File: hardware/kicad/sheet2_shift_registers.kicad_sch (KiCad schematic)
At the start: 0 parts

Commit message: feat: populate all 4 KiCad schematic sheets with embedded symbols and wiring
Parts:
- added U1, U2, U3, U4, U5, U6, U7, U8: 74HC595, symbol HPVE:74HC595
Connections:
- new net +3V3: U1.14 (SER), U2.14 (SER), U3.14 (SER), U4.14 (SER), U5.14 (SER), U6.14 (SER), U7.14 (SER), U8.14 (SER)
- new net CASCADE_1: U2.10 (~{SRCLR})
- new net CASCADE_2: U3.10 (~{SRCLR})
- new net CASCADE_3: U4.10 (~{SRCLR})
- new net CASCADE_4: U5.10 (~{SRCLR})
- new net CASCADE_5: U6.10 (~{SRCLR})
- new net CASCADE_6: U7.10 (~{SRCLR})
- new net CASCADE_7: U8.10 (~{SRCLR})
- new net GND: U1.11 (SRCLK), U2.11 (SRCLK), U3.11 (SRCLK), U4.11 (SRCLK), U5.11 (SRCLK), U6.11 (SRCLK), U7.11 (SRCLK), U8.11 (SRCLK)
- new net SPI_LATCH: U1.12 (RCLK), U2.12 (RCLK), U3.12 (RCLK), U4.12 (RCLK), U5.12 (RCLK), U6.12 (RCLK), U7.12 (RCLK), U8.12 (RCLK)
- new net SPI_MOSI: U1.10 (~{SRCLR})
- new net SPI_SCK: U1.13 (~{OE}), U2.13 (~{OE}), U3.13 (~{OE}), U4.13 (~{OE}), U5.13 (~{OE}), U6.13 (~{OE}), U7.13 (~{OE}), U8.13 (~{OE})
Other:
- title: Sheet 2: 74HC595 Shift Register Cascade -> Sheet 2: 74HC595 High-Speed Shift Register Cascade (8 Stages)

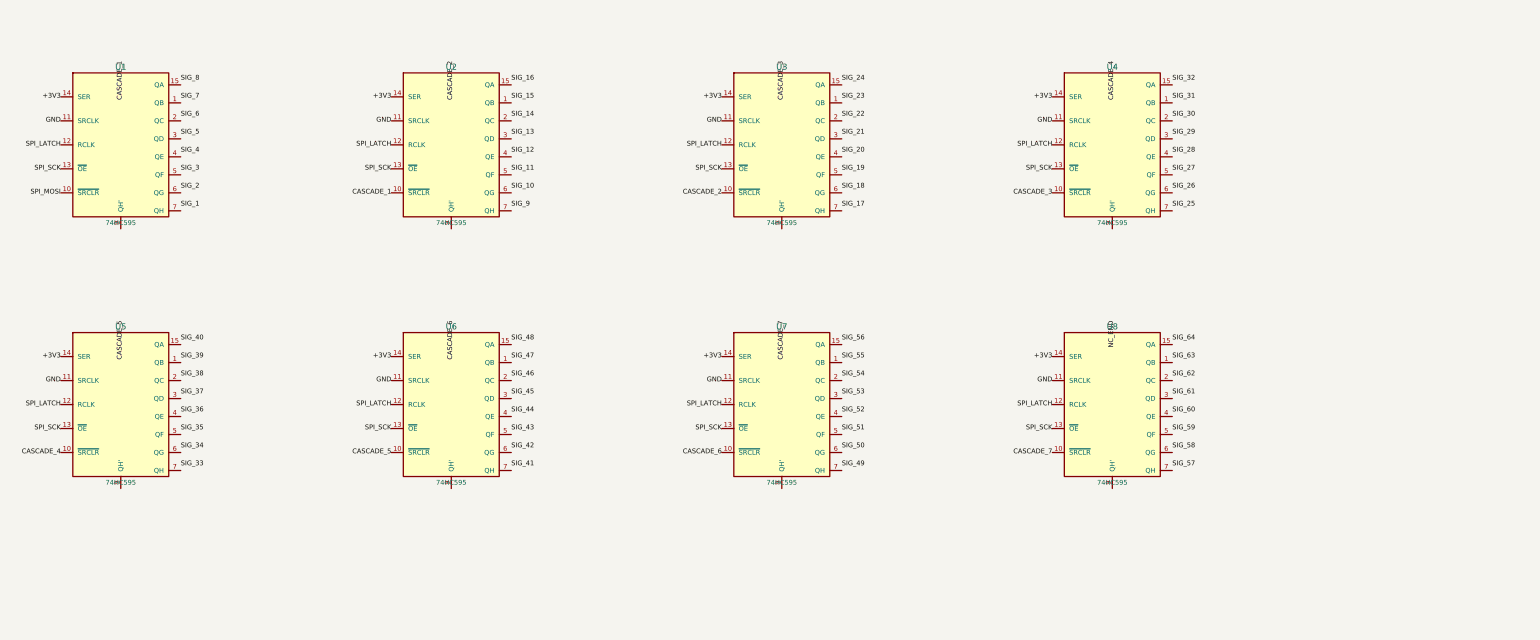
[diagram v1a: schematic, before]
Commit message: fix(kicad): assign valid footprints to all 105 symbols and add visible wiring
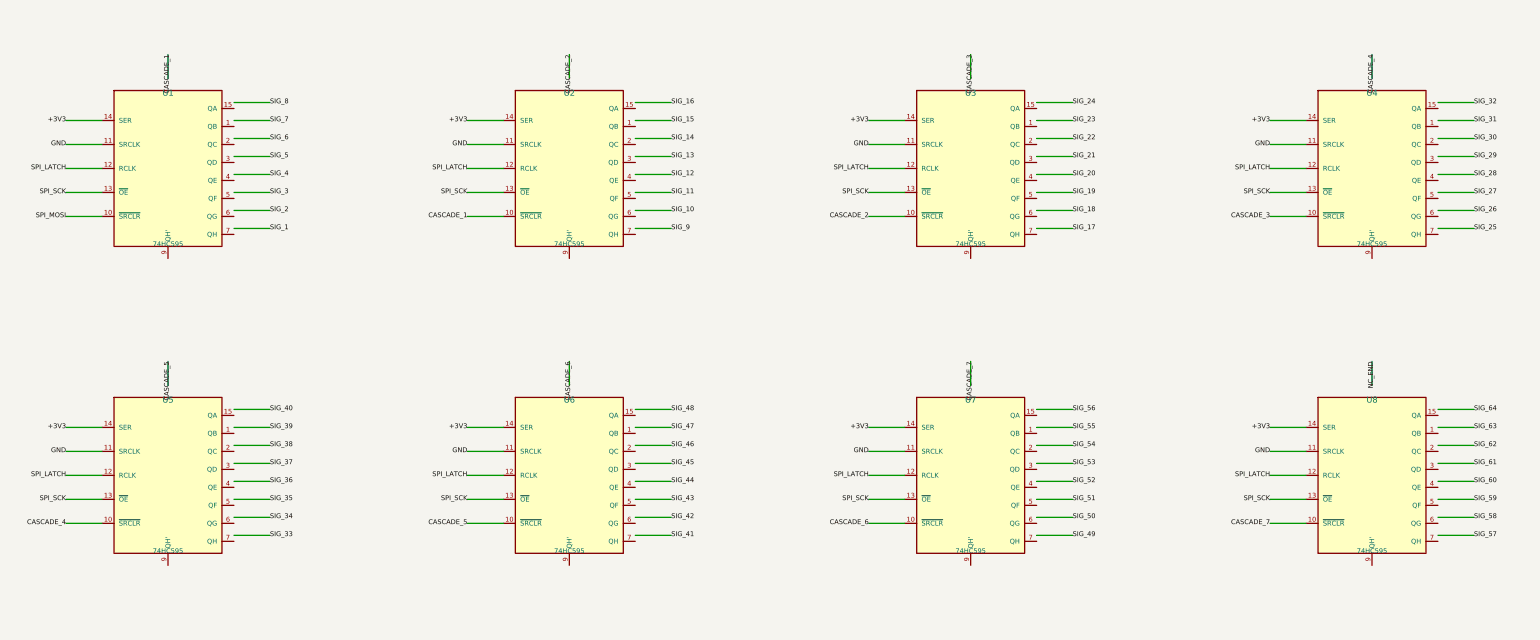
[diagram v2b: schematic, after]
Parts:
- U1, U2, U3, U4, U5, U6, U7, U8: footprint (none) -> Package_DIP:DIP-16_W7.62mm

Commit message: Update KiCad symbols and netlist for spotless F8 PCB sync
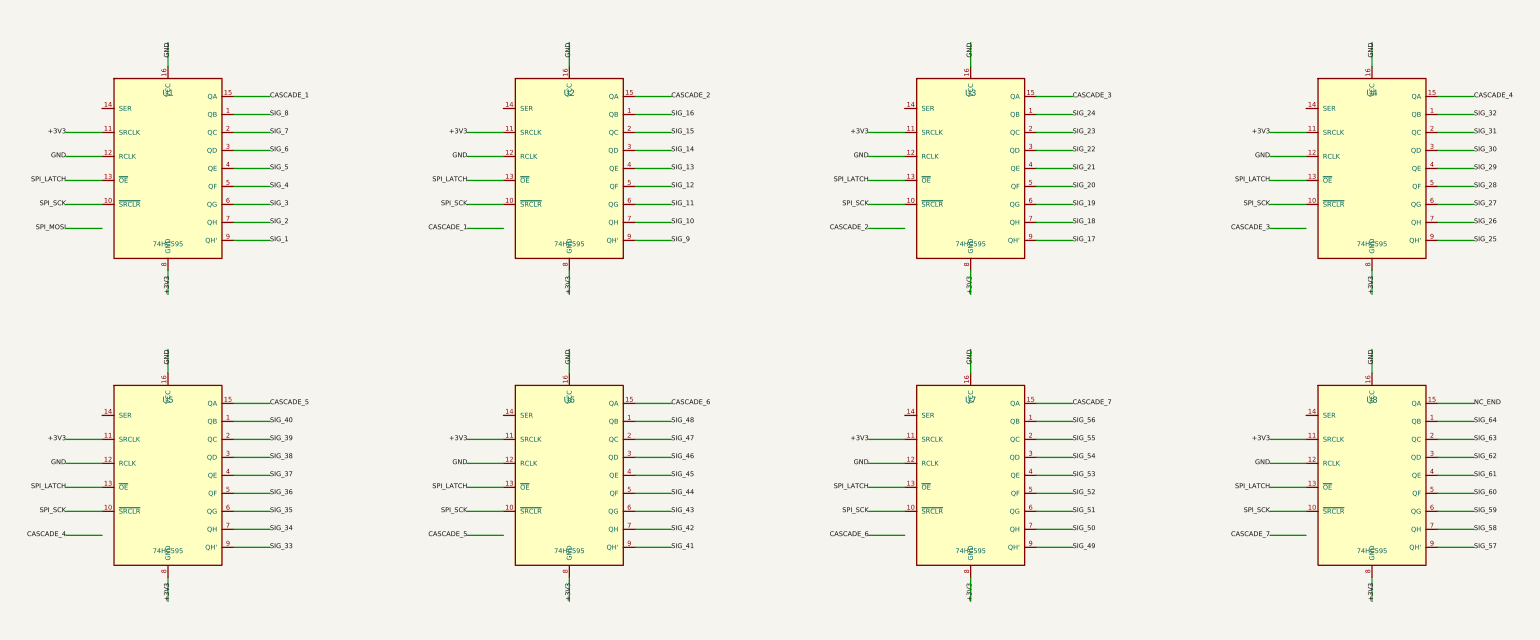
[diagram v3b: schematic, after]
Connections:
- net +3V3: now also U1.11 (SRCLK), U1.8 (GND), U2.11 (SRCLK), U2.8 (GND), U3.11 (SRCLK), U3.8 (GND), U4.11 (SRCLK), U4.8 (GND), U5.11 (SRCLK), U5.8 (GND), U6.11 (SRCLK), U6.8 (GND), U7.11 (SRCLK), U7.8 (GND), U8.11 (SRCLK), U8.8 (GND); no longer U1.14 (SER), U2.14 (SER), U3.14 (SER), U4.14 (SER), U5.14 (SER), U6.14 (SER), U7.14 (SER), U8.14 (SER)
- net CASCADE_1: now also U1.15 (QA); no longer U2.10 (~{SRCLR})
- net CASCADE_2: now also U2.15 (QA); no longer U3.10 (~{SRCLR})
- net CASCADE_3: now also U3.15 (QA); no longer U4.10 (~{SRCLR})
- net CASCADE_4: now also U4.15 (QA); no longer U5.10 (~{SRCLR})
- net CASCADE_5: now also U5.15 (QA); no longer U6.10 (~{SRCLR})
- net CASCADE_6: now also U6.15 (QA); no longer U7.10 (~{SRCLR})
- net CASCADE_7: now also U7.15 (QA); no longer U8.10 (~{SRCLR})
- net GND: now also U1.12 (RCLK), U1.16 (VCC), U2.12 (RCLK), U2.16 (VCC), U3.12 (RCLK), U3.16 (VCC), U4.12 (RCLK), U4.16 (VCC), U5.12 (RCLK), U5.16 (VCC), U6.12 (RCLK), U6.16 (VCC), U7.12 (RCLK), U7.16 (VCC), U8.12 (RCLK), U8.16 (VCC); no longer U1.11 (SRCLK), U2.11 (SRCLK), U3.11 (SRCLK), U4.11 (SRCLK), U5.11 (SRCLK), U6.11 (SRCLK), U7.11 (SRCLK), U8.11 (SRCLK)
- net NC_END: now also U8.15 (QA)
- net SIG_1: now also U1.9 (QH')
- net SIG_10: now also U2.7 (QH)
- net SIG_11: now also U2.6 (QG)
- net SIG_12: now also U2.5 (QF)
- net SIG_13: now also U2.4 (QE)
- net SIG_14: now also U2.3 (QD)
- net SIG_15: now also U2.2 (QC)
- net SIG_16: now also U2.1 (QB)
- net SIG_17: now also U3.9 (QH')
- net SIG_18: now also U3.7 (QH)
- net SIG_19: now also U3.6 (QG)
- net SIG_2: now also U1.7 (QH)
- net SIG_20: now also U3.5 (QF)
- net SIG_21: now also U3.4 (QE)
- net SIG_22: now also U3.3 (QD)
- net SIG_23: now also U3.2 (QC)
- net SIG_24: now also U3.1 (QB)
- net SIG_25: now also U4.9 (QH')
- net SIG_26: now also U4.7 (QH)
- net SIG_27: now also U4.6 (QG)
- net SIG_28: now also U4.5 (QF)
- net SIG_29: now also U4.4 (QE)
- net SIG_3: now also U1.6 (QG)
- net SIG_30: now also U4.3 (QD)
- net SIG_31: now also U4.2 (QC)
- net SIG_32: now also U4.1 (QB)
- net SIG_33: now also U5.9 (QH')
- net SIG_34: now also U5.7 (QH)
- net SIG_35: now also U5.6 (QG)
- net SIG_36: now also U5.5 (QF)
- net SIG_37: now also U5.4 (QE)
- net SIG_38: now also U5.3 (QD)
- net SIG_39: now also U5.2 (QC)
- net SIG_4: now also U1.5 (QF)
- net SIG_40: now also U5.1 (QB)
- net SIG_41: now also U6.9 (QH')
- net SIG_42: now also U6.7 (QH)
- net SIG_43: now also U6.6 (QG)
- net SIG_44: now also U6.5 (QF)
- net SIG_45: now also U6.4 (QE)
- net SIG_46: now also U6.3 (QD)
- net SIG_47: now also U6.2 (QC)
- net SIG_48: now also U6.1 (QB)
- net SIG_49: now also U7.9 (QH')
- net SIG_5: now also U1.4 (QE)
- net SIG_50: now also U7.7 (QH)
- net SIG_51: now also U7.6 (QG)
- net SIG_52: now also U7.5 (QF)
- net SIG_53: now also U7.4 (QE)
- net SIG_54: now also U7.3 (QD)
- net SIG_55: now also U7.2 (QC)
- net SIG_56: now also U7.1 (QB)
- net SIG_57: now also U8.9 (QH')
- net SIG_58: now also U8.7 (QH)
- net SIG_59: now also U8.6 (QG)
- net SIG_6: now also U1.3 (QD)
- net SIG_60: now also U8.5 (QF)
- net SIG_61: now also U8.4 (QE)
- net SIG_62: now also U8.3 (QD)
- net SIG_63: now also U8.2 (QC)
- net SIG_64: now also U8.1 (QB)
- net SIG_7: now also U1.2 (QC)
- net SIG_8: now also U1.1 (QB)
- net SIG_9: now also U2.9 (QH')
- net SPI_LATCH: now also U1.13 (~{OE}), U2.13 (~{OE}), U3.13 (~{OE}), U4.13 (~{OE}), U5.13 (~{OE}), U6.13 (~{OE}), U7.13 (~{OE}), U8.13 (~{OE}); no longer U1.12 (RCLK), U2.12 (RCLK), U3.12 (RCLK), U4.12 (RCLK), U5.12 (RCLK), U6.12 (RCLK), U7.12 (RCLK), U8.12 (RCLK)
- net SPI_MOSI: no longer U1.10 (~{SRCLR})
- net SPI_SCK: now also U1.10 (~{SRCLR}), U2.10 (~{SRCLR}), U3.10 (~{SRCLR}), U4.10 (~{SRCLR}), U5.10 (~{SRCLR}), U6.10 (~{SRCLR}), U7.10 (~{SRCLR}), U8.10 (~{SRCLR}); no longer U1.13 (~{OE}), U2.13 (~{OE}), U3.13 (~{OE}), U4.13 (~{OE}), U5.13 (~{OE}), U6.13 (~{OE}), U7.13 (~{OE}), U8.13 (~{OE})

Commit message: Auto-route 392 copper tracks for 64-channel HPVE phased array PCB
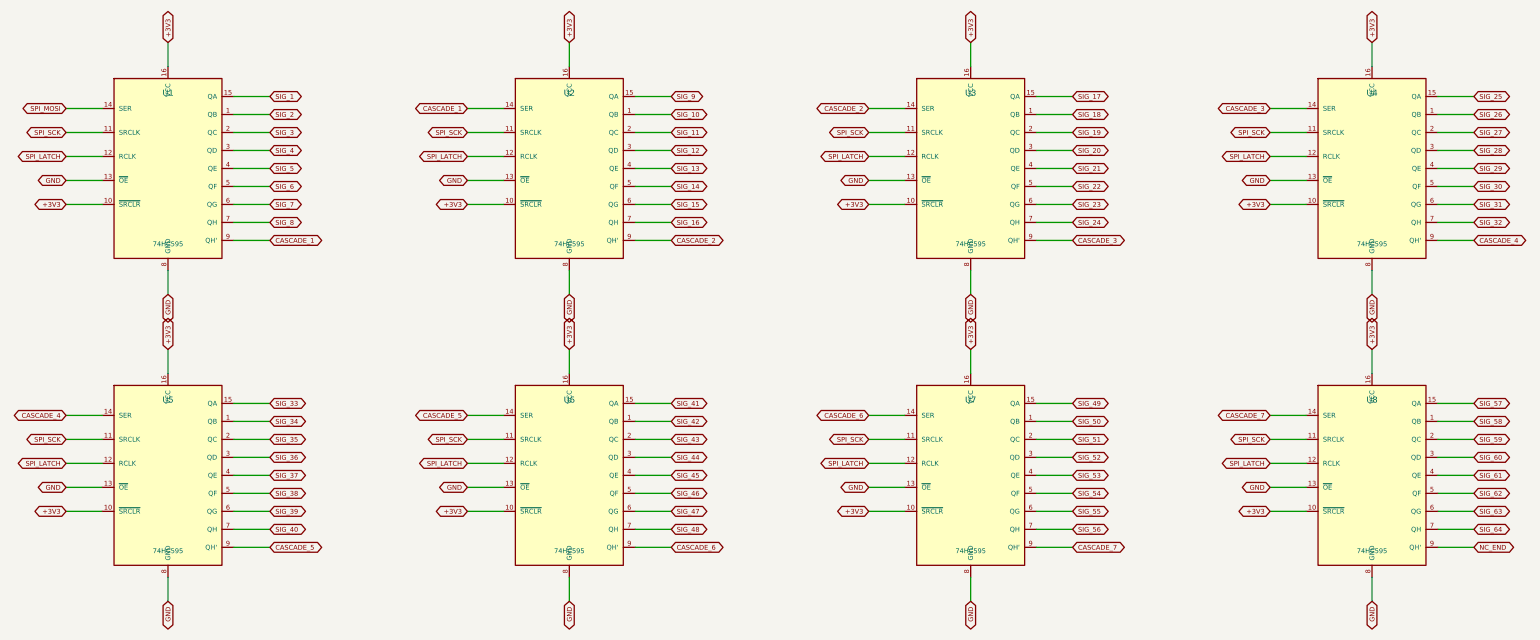
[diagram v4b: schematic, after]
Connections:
- net +3V3: now also U1.10 (~{SRCLR}), U1.16 (VCC), U2.10 (~{SRCLR}), U2.16 (VCC), U3.10 (~{SRCLR}), U3.16 (VCC), U4.10 (~{SRCLR}), U4.16 (VCC), U5.10 (~{SRCLR}), U5.16 (VCC), U6.10 (~{SRCLR}), U6.16 (VCC), U7.10 (~{SRCLR}), U7.16 (VCC), U8.10 (~{SRCLR}), U8.16 (VCC); no longer U1.11 (SRCLK), U1.8 (GND), U2.11 (SRCLK), U2.8 (GND), U3.11 (SRCLK), U3.8 (GND), U4.11 (SRCLK), U4.8 (GND), U5.11 (SRCLK), U5.8 (GND), U6.11 (SRCLK), U6.8 (GND), U7.11 (SRCLK), U7.8 (GND), U8.11 (SRCLK), U8.8 (GND)
- net CASCADE_1: now also U1.9 (QH'), U2.14 (SER); no longer U1.15 (QA)
- net CASCADE_2: now also U2.9 (QH'), U3.14 (SER); no longer U2.15 (QA)
- net CASCADE_3: now also U3.9 (QH'), U4.14 (SER); no longer U3.15 (QA)
- net CASCADE_4: now also U4.9 (QH'), U5.14 (SER); no longer U4.15 (QA)
- net CASCADE_5: now also U5.9 (QH'), U6.14 (SER); no longer U5.15 (QA)
- net CASCADE_6: now also U6.9 (QH'), U7.14 (SER); no longer U6.15 (QA)
- net CASCADE_7: now also U7.9 (QH'), U8.14 (SER); no longer U7.15 (QA)
- net GND: now also U1.13 (~{OE}), U1.8 (GND), U2.13 (~{OE}), U2.8 (GND), U3.13 (~{OE}), U3.8 (GND), U4.13 (~{OE}), U4.8 (GND), U5.13 (~{OE}), U5.8 (GND), U6.13 (~{OE}), U6.8 (GND), U7.13 (~{OE}), U7.8 (GND), U8.13 (~{OE}), U8.8 (GND); no longer U1.12 (RCLK), U1.16 (VCC), U2.12 (RCLK), U2.16 (VCC), U3.12 (RCLK), U3.16 (VCC), U4.12 (RCLK), U4.16 (VCC), U5.12 (RCLK), U5.16 (VCC), U6.12 (RCLK), U6.16 (VCC), U7.12 (RCLK), U7.16 (VCC), U8.12 (RCLK), U8.16 (VCC)
- net NC_END: now also U8.9 (QH'); no longer U8.15 (QA)
- net SIG_1: now also U1.15 (QA); no longer U1.9 (QH')
- net SIG_10: now also U2.1 (QB); no longer U2.7 (QH)
- net SIG_11: now also U2.2 (QC); no longer U2.6 (QG)
- net SIG_12: now also U2.3 (QD); no longer U2.5 (QF)
- net SIG_14: now also U2.5 (QF); no longer U2.3 (QD)
- net SIG_15: now also U2.6 (QG); no longer U2.2 (QC)
- net SIG_16: now also U2.7 (QH); no longer U2.1 (QB)
- net SIG_17: now also U3.15 (QA); no longer U3.9 (QH')
- net SIG_18: now also U3.1 (QB); no longer U3.7 (QH)
- net SIG_19: now also U3.2 (QC); no longer U3.6 (QG)
- net SIG_2: now also U1.1 (QB); no longer U1.7 (QH)
- net SIG_20: now also U3.3 (QD); no longer U3.5 (QF)
- net SIG_22: now also U3.5 (QF); no longer U3.3 (QD)
- net SIG_23: now also U3.6 (QG); no longer U3.2 (QC)
- net SIG_24: now also U3.7 (QH); no longer U3.1 (QB)
- net SIG_25: now also U4.15 (QA); no longer U4.9 (QH')
- net SIG_26: now also U4.1 (QB); no longer U4.7 (QH)
- net SIG_27: now also U4.2 (QC); no longer U4.6 (QG)
- net SIG_28: now also U4.3 (QD); no longer U4.5 (QF)
- net SIG_3: now also U1.2 (QC); no longer U1.6 (QG)
- net SIG_30: now also U4.5 (QF); no longer U4.3 (QD)
- net SIG_31: now also U4.6 (QG); no longer U4.2 (QC)
- net SIG_32: now also U4.7 (QH); no longer U4.1 (QB)
- net SIG_33: now also U5.15 (QA); no longer U5.9 (QH')
- net SIG_34: now also U5.1 (QB); no longer U5.7 (QH)
- net SIG_35: now also U5.2 (QC); no longer U5.6 (QG)
- net SIG_36: now also U5.3 (QD); no longer U5.5 (QF)
- net SIG_38: now also U5.5 (QF); no longer U5.3 (QD)
- net SIG_39: now also U5.6 (QG); no longer U5.2 (QC)
- net SIG_4: now also U1.3 (QD); no longer U1.5 (QF)
- net SIG_40: now also U5.7 (QH); no longer U5.1 (QB)
- net SIG_41: now also U6.15 (QA); no longer U6.9 (QH')
- net SIG_42: now also U6.1 (QB); no longer U6.7 (QH)
- net SIG_43: now also U6.2 (QC); no longer U6.6 (QG)
- net SIG_44: now also U6.3 (QD); no longer U6.5 (QF)
- net SIG_46: now also U6.5 (QF); no longer U6.3 (QD)
- net SIG_47: now also U6.6 (QG); no longer U6.2 (QC)
- net SIG_48: now also U6.7 (QH); no longer U6.1 (QB)
- net SIG_49: now also U7.15 (QA); no longer U7.9 (QH')
- net SIG_50: now also U7.1 (QB); no longer U7.7 (QH)
- net SIG_51: now also U7.2 (QC); no longer U7.6 (QG)
- net SIG_52: now also U7.3 (QD); no longer U7.5 (QF)
- net SIG_54: now also U7.5 (QF); no longer U7.3 (QD)
- net SIG_55: now also U7.6 (QG); no longer U7.2 (QC)
- net SIG_56: now also U7.7 (QH); no longer U7.1 (QB)
- net SIG_57: now also U8.15 (QA); no longer U8.9 (QH')
- net SIG_58: now also U8.1 (QB); no longer U8.7 (QH)
- net SIG_59: now also U8.2 (QC); no longer U8.6 (QG)
- net SIG_6: now also U1.5 (QF); no longer U1.3 (QD)
- net SIG_60: now also U8.3 (QD); no longer U8.5 (QF)
- net SIG_62: now also U8.5 (QF); no longer U8.3 (QD)
- net SIG_63: now also U8.6 (QG); no longer U8.2 (QC)
- net SIG_64: now also U8.7 (QH); no longer U8.1 (QB)
- net SIG_7: now also U1.6 (QG); no longer U1.2 (QC)
- net SIG_8: now also U1.7 (QH); no longer U1.1 (QB)
- net SIG_9: now also U2.15 (QA); no longer U2.9 (QH')
- net SPI_LATCH: now also U1.12 (RCLK), U2.12 (RCLK), U3.12 (RCLK), U4.12 (RCLK), U5.12 (RCLK), U6.12 (RCLK), U7.12 (RCLK), U8.12 (RCLK); no longer U1.13 (~{OE}), U2.13 (~{OE}), U3.13 (~{OE}), U4.13 (~{OE}), U5.13 (~{OE}), U6.13 (~{OE}), U7.13 (~{OE}), U8.13 (~{OE})
- net SPI_MOSI: now also U1.14 (SER)
- net SPI_SCK: now also U1.11 (SRCLK), U2.11 (SRCLK), U3.11 (SRCLK), U4.11 (SRCLK), U5.11 (SRCLK), U6.11 (SRCLK), U7.11 (SRCLK), U8.11 (SRCLK); no longer U1.10 (~{SRCLR}), U2.10 (~{SRCLR}), U3.10 (~{SRCLR}), U4.10 (~{SRCLR}), U5.10 (~{SRCLR}), U6.10 (~{SRCLR}), U7.10 (~{SRCLR}), U8.10 (~{SRCLR})
